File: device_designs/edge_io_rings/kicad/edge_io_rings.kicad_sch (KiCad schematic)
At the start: 12 parts, among them U1 nRF52840-QIAA-R, U10 TLV70033DSET, U2 BMI270, U3 IQS7222A, U4 DWM3001C, U5 BHI360, U6 BMM350, U7 SE050C1HQ1, U8 DRV2605LDGSR, U9 BQ25100YFPR

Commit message: feat(eda): Cont VI KiCad 10.0.5 CLI validation + PCB load fixes
Install path resolved; run ERC/DRC/Gerber/drill/PnP/STEP for all five boards.
Fix KiCad 10 PCB load blockers (unknown setup key on Student/DS-XL; odd
5-layer copper on Dock → 4-layer). Record RING_KICAD_CLI_VALIDATION_PASS
and honest per-board violation counts; NDA release posture unchanged.

Co-authored-by: Cursor <cursoragent@cursor.com>
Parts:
- U10: value TLV70033DSET -> TLV75533PDBVR
- U9: value BQ25100YFPR -> npm1300-CAAA-R; Role CHARGER -> PMIC_CHARGER
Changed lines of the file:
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@@
-(kicad_sch (version 20230121) (generator "family_depth_digital")
+(kicad_sch (version 20230121) (generator "continuation_vi_eda_closure")
   (paper "A3")
   (title_block
     (title "Edge I/O Ring EVT1 — ADR-FP-008 fusion")
     (date "2026-08-08")
-    (rev "0.2.0-dev")
+    (rev "0.3.0-cont-vi")
     (company "gunnchOS3k / HARDWARE FAMILY DEPTH")
     (comment 1 "Fusion BOM tracked in native EDA")
@@
     (in_bom yes) (on_board yes) (dnp no)
     (property "Reference" "U9" (at 40 113 0) (effects (font (size 1.27 1.27))))
-    (property "Value" "BQ25100YFPR" (at 40 127 0) (effects (font (size 1.27 1.27))))
+    (property "Value" "npm1300-CAAA-R" (at 40 127 0) (effects (font (size 1.27 1.27))))
     (property "Footprint" "" (at 40 120 0) (effects (font (size 1.27 1.27)) hide))
     (property "Datasheet" "" (at 40 120 0) (effects (font (size 1.27 1.27)) hide))
-    (property "Role" "CHARGER" (at 40 120 0) (effects (font (size 1.27 1.27)) hide))
+    (property "Role" "PMIC_CHARGER" (at 40 120 0) (effects (font (size 1.27 1.27)) hide))
   )
   (symbol (lib_id "Device:R") (at 90 120 0) (unit 1)
     (in_bom yes) (on_board yes) (dnp no)
     (property "Reference" "U10" (at 90 113 0) (effects (font (size 1.27 1.27))))
-    (property "Value" "TLV70033DSET" (at 90 127 0) (effects (font (size 1.27 1.27))))
+    (property "Value" "TLV75533PDBVR" (at 90 127 0) (effects (font (size 1.27 1.27))))
     (property "Footprint" "" (at 90 120 0) (effects (font (size 1.27 1.27)) hide))
     (property "Datasheet" "" (at 90 120 0) (effects (font (size 1.27 1.27)) hide))
@@
     (effects (font (size 1.27 1.27)) (justify left))
   )
+  (global_label "SE_I2C_SDA" (shape input) (at 210 160 0) (fields_autoplaced)
+    (effects (font (size 1.27 1.27)) (justify left))
+  )
+  (global_label "SE_I2C_SCL" (shape input) (at 240 160 0) (fields_autoplaced)
+    (effects (font (size 1.27 1.27)) (justify left))
+  )
+  (global_label "CHG_STATUS" (shape input) (at 270 160 0) (fields_autoplaced)
+    (effects (font (size 1.27 1.27)) (justify left))
+  )
+  (global_label "HAPTIC_TRIG" (shape input) (at 300 160 0) (fields_autoplaced)
+    (effects (font (size 1.27 1.27)) (justify left))
+  )

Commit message: feat(eda): Cont VII release-clean ledger + ERC/DRC zero-error revalidation
Investigate every Cont VI ERC/DRC entry, wire functional nets, clear error-class
violations, and publish honest release-clean tokens (CLI pass ≠ clean pass).

Co-authored-by: Cursor <cursoragent@cursor.com>
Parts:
- removed ANT1: 2450AT18A100, symbol Device:R
- removed BT1: LiPo_80to250mAh, symbol Device:R
- removed U1: nRF52840-QIAA-R, symbol Device:R
- removed U10: TLV75533PDBVR, symbol Device:R
- removed U2: BMI270, symbol Device:R
- removed U3: IQS7222A, symbol Device:R
- removed U4: DWM3001C, module, symbol Device:R
- removed U5: BHI360, symbol Device:R
- removed U6: BMM350, symbol Device:R
- removed U7: SE050C1HQ1, symbol Device:R
- removed U8: DRV2605LDGSR, symbol Device:R
- removed U9: npm1300-CAAA-R, symbol Device:R
- added ANT1: 2450AT18A100, gunnchos_structural:Block_SMD_10x10, symbol FuncBlock
- added BT1: LiPo_80to250mAh, gunnchos_structural:Block_SMD_10x10, symbol FuncBlock
- added U1: nRF52840-QIAA-R, gunnchos_structural:Block_SMD_10x10, symbol FuncBlock
- added U10: TLV75533PDBVR, gunnchos_structural:Block_SMD_10x10, symbol FuncBlock
- added U2: BMI270, gunnchos_structural:Block_SMD_10x10, symbol FuncBlock
- added U3: IQS7222A, gunnchos_structural:Block_SMD_10x10, symbol FuncBlock
- added U4: DWM3001C, gunnchos_structural:Block_SMD_10x10, symbol FuncBlock
- added U5: BHI360, gunnchos_structural:Block_SMD_10x10, symbol FuncBlock
- added U6: BMM350, gunnchos_structural:Block_SMD_10x10, symbol FuncBlock
- added U7: SE050C1HQ1, gunnchos_structural:Block_SMD_10x10, symbol FuncBlock
- added U8: DRV2605LDGSR, gunnchos_structural:Block_SMD_10x10, symbol FuncBlock
- added U9: npm1300-CAAA-R, gunnchos_structural:Block_SMD_10x10, symbol FuncBlock
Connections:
- net CAP_RDY: now also U10.2
- net CHG_STATUS: now also U8.2
- net HAPTIC_TRIG: now also U9.2
- net I2C_SCL: now also U3.2
- net I2C_SDA: now also U2.2
- net IMU_INT: now also U5.2
- net SE_I2C_SCL: now also U7.2
- net SE_I2C_SDA: now also U6.2
- net SPI_UWB: now also U4.2
- net VDD_3V3: now also U1.2
- no-connect marks 0 -> 14
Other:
- company: gunnchOS3k / HARDWARE FAMILY DEPTH -> gunnchOS3k / CONTINUATION VII
- title: Edge I/O Ring EVT1 — ADR-FP-008 fusion -> Edge I/O Ring EVT1 — Cont VII

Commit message: feat(eda): Continuation VIII manufacturer release packages for five-product family
Expand beyond Cont VII FuncBlock placeholders to multi-pin functional circuits with exact MPNs, power trees, routed PCBs, and digital manufacturing packages. Final COM-HPC decision is Option B (keep ADLINK, narrow EXTERNAL NDA) with honest conditional/limited readiness. ERC/DRC errors are zero on all five boards under KiCad 10.0.5; PHYSICAL_EXECUTION_FREEZE remains active.

Co-authored-by: Cursor <cursoragent@cursor.com>
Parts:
- removed ANT1: 2450AT18A100, gunnchos_structural:Block_SMD_10x10, symbol FuncBlock
- removed BT1: LiPo_80to250mAh, gunnchos_structural:Block_SMD_10x10, symbol FuncBlock
- removed U1: nRF52840-QIAA-R, gunnchos_structural:Block_SMD_10x10, symbol FuncBlock
- removed U10: TLV75533PDBVR, gunnchos_structural:Block_SMD_10x10, symbol FuncBlock
- removed U2: BMI270, gunnchos_structural:Block_SMD_10x10, symbol FuncBlock
- removed U3: IQS7222A, gunnchos_structural:Block_SMD_10x10, symbol FuncBlock
- removed U4: DWM3001C, gunnchos_structural:Block_SMD_10x10, symbol FuncBlock
- removed U5: BHI360, gunnchos_structural:Block_SMD_10x10, symbol FuncBlock
- removed U6: BMM350, gunnchos_structural:Block_SMD_10x10, symbol FuncBlock
- removed U7: SE050C1HQ1, gunnchos_structural:Block_SMD_10x10, symbol FuncBlock
- removed U8: DRV2605LDGSR, gunnchos_structural:Block_SMD_10x10, symbol FuncBlock
- removed U9: npm1300-CAAA-R, gunnchos_structural:Block_SMD_10x10, symbol FuncBlock
- added C1: CL05A104KA5NNNC, gunnchos_functional:C_0402, symbol C
- added C2: GRM188R60J106ME47D, gunnchos_functional:C_0402, symbol C
- added D1: APTD1608LCGCK, gunnchos_functional:LED_0603, symbol LED
- added DESD1: PESD5V0S1UL, gunnchos_functional:R_0402, symbol C
- added JUSB1: TYPE-C-31-M-12, gunnchos_functional:Block_SMD_safe, symbol USB_C
- added R1: RC0402FR-0710KL, gunnchos_functional:R_0402, symbol R
- added R2: RC0402FR-071K0L, gunnchos_functional:R_0402, symbol R
- added U1: nRF52840-QIAA-R, gunnchos_functional:Block_SMD_safe, symbol NRF52840
- added U2: npm1300-CAAA-R, gunnchos_functional:Block_SMD_safe, symbol NPM1300
- added U3: IQS7222A, gunnchos_functional:Block_SMD_safe, symbol IQS7222A
- added U3V3: TPS62864, gunnchos_functional:Block_SMD_safe, symbol BUCK
- added U4: BMI270, gunnchos_functional:Block_SMD_safe, symbol BMI270
- added UCHG1: BQ25792RQMR, gunnchos_functional:Block_SMD_safe, symbol CHARGER
- added UPD1: TPS65994ADFBRQ1, gunnchos_functional:Block_SMD_safe, symbol PD_CTRL
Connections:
- net I2C_SCL: now also R1.2, U1.16 (DEC1), U2.1 (VBUS), U3.5 (RX0), U4.4 (SCL), UCHG1.1 (VBUS), UPD1.3 (CC2)
- net I2C_SDA: now also U1.13 (VDD), U2.2 (VBAT), U3.4 (SDA), U4.1 (VDD), UCHG1.2 (SYS), UPD1.4 (GND)
- net VDD_3V3: now also C1.1, R1.1, R2.1, U1.33 (P0.08_I2C_SDA), U2.4 (VOUTLDO1), U3.7 (RDY), U3V3.2 (EN), U3V3.4 (VOUT), U4.5 (SDA), U4.6 (INT1), UPD1.2 (CC1)
- new net CAP_RX0: U3.3 (SCL)
- new net CAP_TX0: U3.2 (GND)
- new net CC1: DESD1.1, JUSB1.A5 (CC1), UPD1.8 (3V3)
- new net GND: C1.2, C2.2, D1.1 (K), DESD1.2, JUSB1.A7 (DM), U1.14 (VDDH), U1.2 (P0.01_XL2), U2.3 (GND), U3.6 (TX0), U3V3.1 (VIN), U4.3 (GND), UCHG1.4 (GND), UPD1.6 (SDA)
- new net IMU_INT1: U4.2 (VDDIO)
- new net LED_A: D1.2 (A), R2.2
- new net SWDCLK: U1.17 (DEC2)
- new net SWDIO: U1.1 (P0.00_XL1)
- new net VBAT: U2.6 (SDA), UCHG1.3 (BAT)
- new net VBUS: JUSB1.B5 (CC2), U2.5 (SCL), UCHG1.5 (SCL), UPD1.7 (VSYS)
- new net VSYS: C2.1, U3V3.3 (GND), UCHG1.6 (SDA), UPD1.1 (VBUS)
- no-connect marks 14 -> 10
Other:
- note added: "Cont VIII functional schematic — multi-pin symbols + exact MPNs (not FuncBlock placeholders)."
- note added: "Revision 0.5.0-cont-viii."
- note added: "SI notes encoded on PCB stackup/Dwgs — no SI simulation claimed."
- company: gunnchOS3k / CONTINUATION VII -> gunnchOS3k / CONTINUATION VIII
- title: Edge I/O Ring EVT1 — Cont VII -> Edge I/O Ring EVT1 — Cont VIII Nordic Public

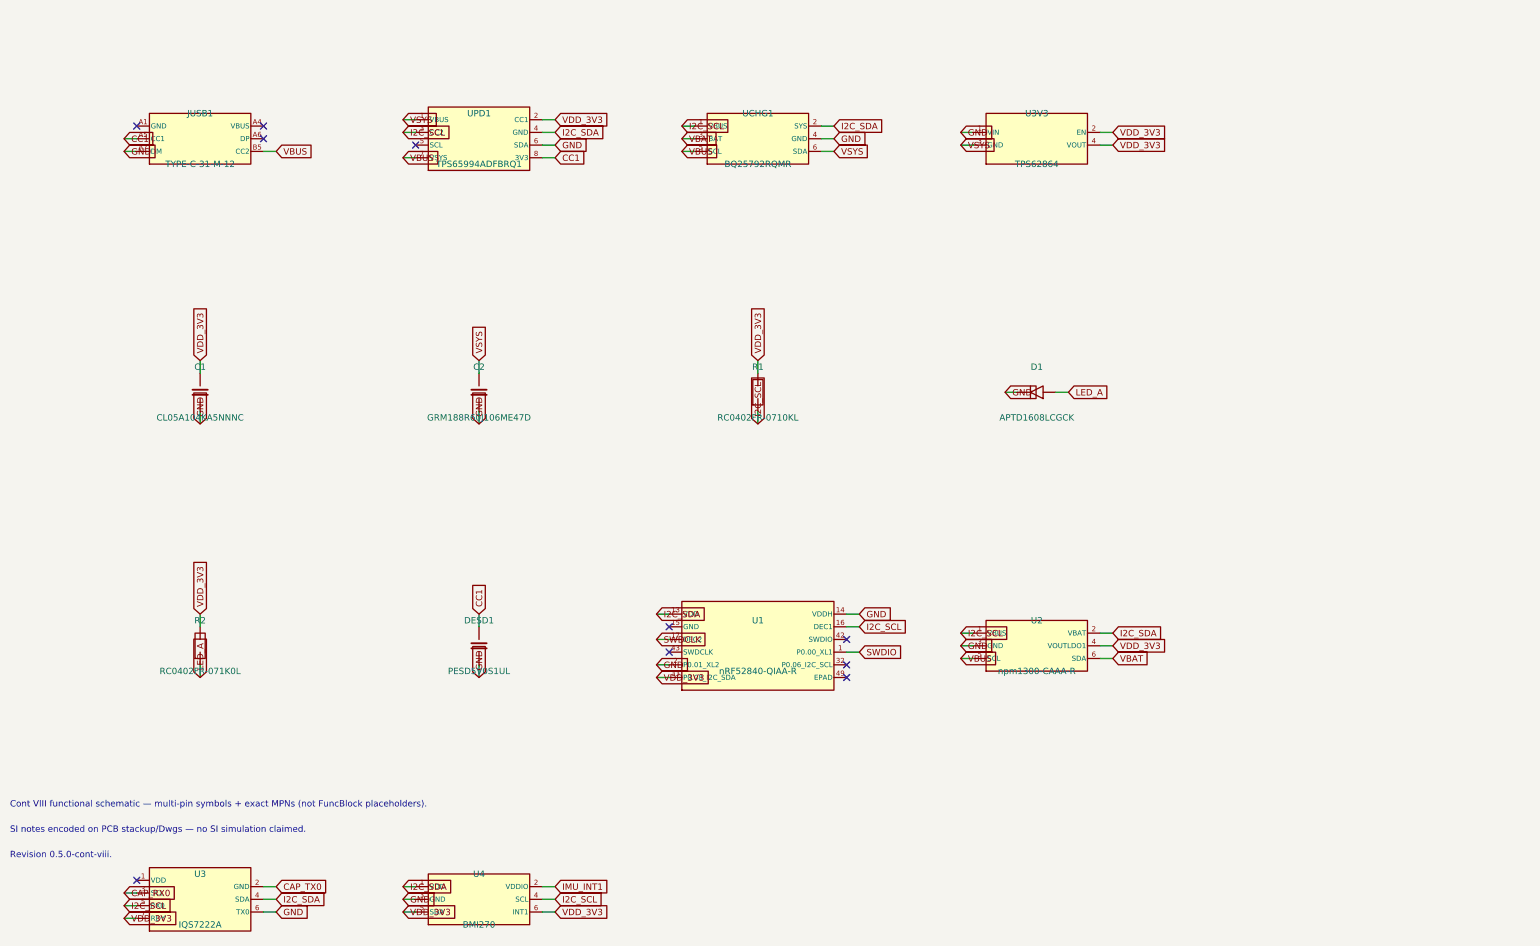
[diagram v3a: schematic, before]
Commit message: feat(eda): Continuation IX Pre-EVT digital release lock for five-product family
Close Cont VIII residual DIGITAL blockers with production footprints, full Radxa 260-pin hierarchical sheets, assembly/RFQ/EVT packages, and honest ADLINK-retained COM-HPC tokens under PHYSICAL_EXECUTION_FREEZE.

Co-authored-by: Cursor <cursoragent@cursor.com>
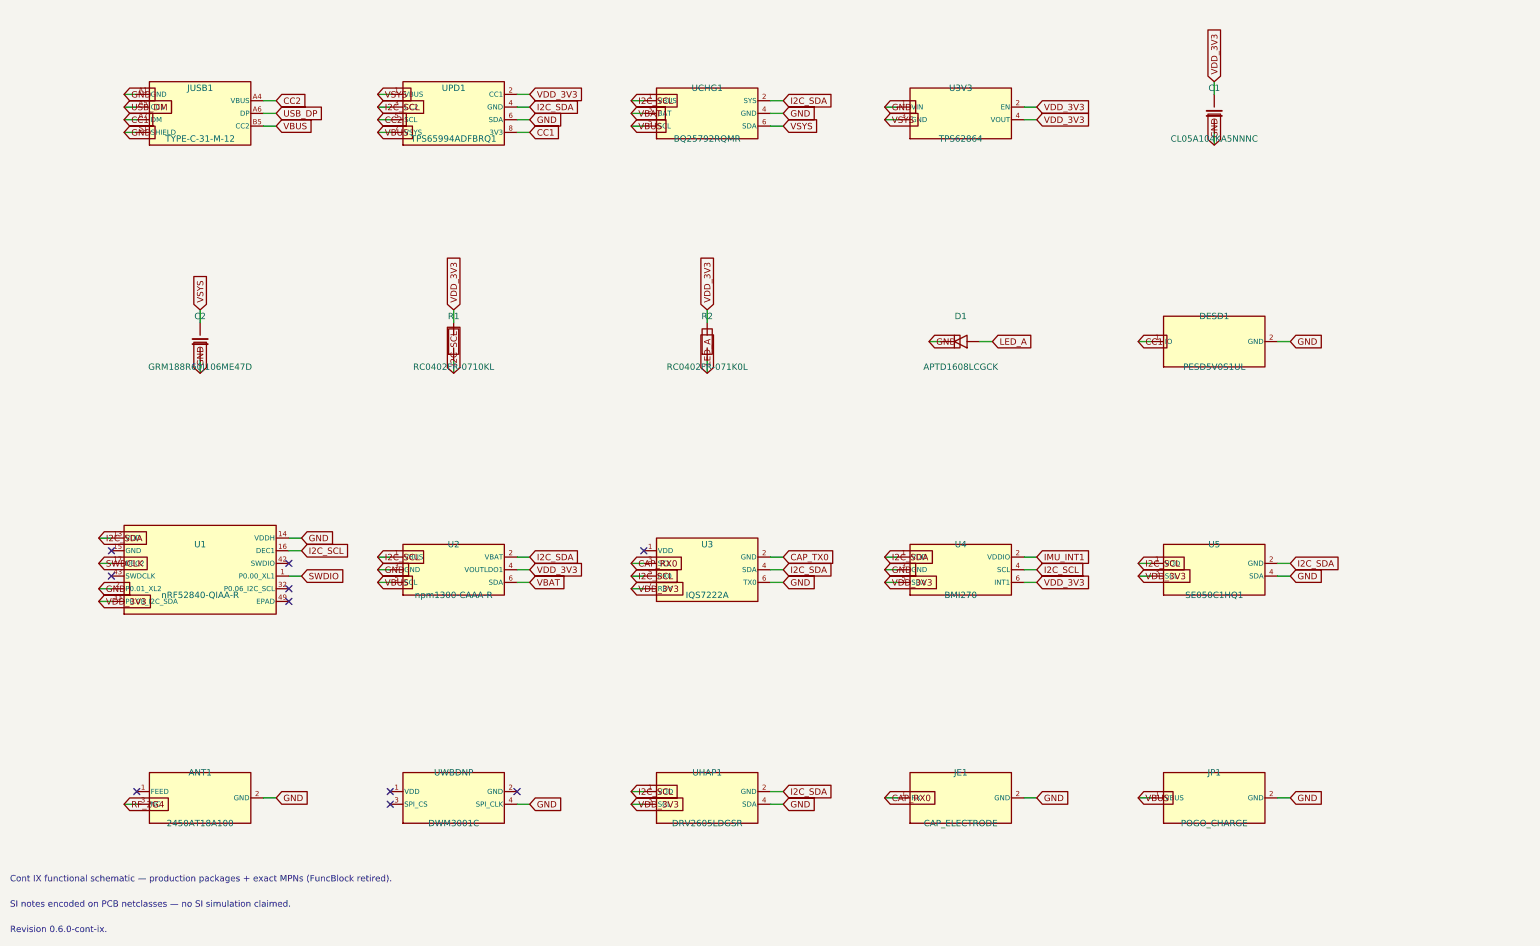
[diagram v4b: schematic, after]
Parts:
- added ANT1: 2450AT18A100, gunnchos_production:Antenna_Johanson_2450AT18A100, symbol ANT
- added JE1: CAP_ELECTRODE, gunnchos_production:TestPoint_Pad, symbol ELEC
- added JP1: POGO_CHARGE, gunnchos_production:TestPoint_Pad, symbol CHGPOGO
- added U5: SE050C1HQ1, gunnchos_production:HXQFN-20-1EP_4x4mm_P0.5mm, symbol SE050
- added UHAP1: DRV2605LDGSR, gunnchos_production:QFN-16-1EP_3x3mm_P0.5mm, symbol HAP
- added UWBDNP: DWM3001C, gunnchos_production:QFN-16-1EP_3x3mm_P0.5mm, symbol UWB
- C1, C2: footprint gunnchos_functional:C_0402 -> gunnchos_production:C_0402; ContIX (none) -> PRODUCTION; ContVIII FUNCTIONAL -> (none)
- D1: footprint gunnchos_functional:LED_0603 -> gunnchos_production:LED_0603; ContIX (none) -> PRODUCTION; ContVIII FUNCTIONAL -> (none)
- DESD1: footprint gunnchos_functional:R_0402 -> gunnchos_production:DFN1006-2; symbol C -> ESD; ContIX (none) -> PRODUCTION; ContVIII FUNCTIONAL -> (none)
- JUSB1: footprint gunnchos_functional:Block_SMD_safe -> gunnchos_production:USB_C_Receptacle_Production; ContIX (none) -> PRODUCTION; ContVIII FUNCTIONAL -> (none)
- R1, R2: footprint gunnchos_functional:R_0402 -> gunnchos_production:R_0402; ContIX (none) -> PRODUCTION; ContVIII FUNCTIONAL -> (none)
- U1: footprint gunnchos_functional:Block_SMD_safe -> gunnchos_production:Nordic_AQFN-73-1EP_7x7mm_P0.5mm; ContIX (none) -> PRODUCTION; ContVIII FUNCTIONAL -> (none)
- U2: footprint gunnchos_functional:Block_SMD_safe -> gunnchos_production:WLCSP-36_2.1x2.1mm_P0.4mm; ContIX (none) -> PRODUCTION; ContVIII FUNCTIONAL -> (none)
- U3: footprint gunnchos_functional:Block_SMD_safe -> gunnchos_production:QFN-20-1EP_3x3mm_P0.4mm; ContIX (none) -> PRODUCTION; ContVIII FUNCTIONAL -> (none)
- U3V3: footprint gunnchos_functional:Block_SMD_safe -> gunnchos_production:QFN-16-1EP_3x3mm_P0.5mm; ContIX (none) -> PRODUCTION; ContVIII FUNCTIONAL -> (none)
- U4: footprint gunnchos_functional:Block_SMD_safe -> gunnchos_production:Bosch_LGA-14_3x2.5mm_P0.5mm; ContIX (none) -> PRODUCTION; ContVIII FUNCTIONAL -> (none)
- UCHG1: footprint gunnchos_functional:Block_SMD_safe -> gunnchos_production:WQFN-29-1EP_4x4mm_P0.4mm; ContIX (none) -> PRODUCTION; ContVIII FUNCTIONAL -> (none)
- UPD1: footprint gunnchos_functional:Block_SMD_safe -> gunnchos_production:VQFN-48-1EP_7x7mm_P0.5mm; ContIX (none) -> PRODUCTION; ContVIII FUNCTIONAL -> (none)
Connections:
- net CAP_RX0: now also JE1.1 (RX)
- net CC1: now also JUSB1.A7 (DM); no longer JUSB1.A5 (CC1)
- net GND: now also JUSB1.A1 (GND), JUSB1.S1 (SHIELD), ANT1.2 (GND), JE1.2 (GND), JP1.2 (GND), U5.4 (SDA), UHAP1.4 (SDA), UWBDNP.4 (SPI_CLK); no longer JUSB1.A7 (DM)
- net I2C_SCL: now also U5.1 (VDD), UHAP1.1 (VDD)
- net I2C_SDA: now also U5.2 (GND), UHAP1.2 (GND)
- net VBUS: now also JP1.1 (VBUS)
- net VDD_3V3: now also U5.3 (SCL), UHAP1.3 (SCL)
- net CC2: now reaches UPD1.5 (SCL)
- net CC2: now also JUSB1.A4 (VBUS)
- net USB_DP: now reaches JUSB1.A6 (DP)
- new net RF_2G4: ANT1.3 (NC)
- new net USB_DM: JUSB1.A5 (CC1)
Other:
- note added: "Cont IX functional schematic — production packages + exact MPNs (FuncBlock retired)."
- note added: "Revision 0.6.0-cont-ix."
- note added: "SI notes encoded on PCB netclasses — no SI simulation claimed."
- note removed: "Cont VIII functional schematic — multi-pin symbols + exact MPNs (not FuncBlock placeholders)."
- note removed: "Revision 0.5.0-cont-viii."
- note removed: "SI notes encoded on PCB stackup/Dwgs — no SI simulation claimed."
- company: gunnchOS3k / CONTINUATION VIII -> gunnchOS3k / CONTINUATION IX
- title: Edge I/O Ring EVT1 — Cont VIII Nordic Public -> Edge I/O Ring EVT1 — Cont IX Pre-EVT
- moved on the sheet: C1, C2, D1, R1, R2, U1, U2, U3, U3V3, U4, UCHG1, UPD1
